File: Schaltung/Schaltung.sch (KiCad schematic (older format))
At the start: 18 parts

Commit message: new annotation
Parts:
- J1: renamed from J?; value Conn_01x02 -> Elektroden
- R1, R2: renamed from R?; value R -> 0,86
- gave numbers to parts that had none: 15
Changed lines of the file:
@@
 $EndDescr
 $Comp
-L +12V #PWR?
+L +12V #PWR1
 U 1 1 5ABA1DC9
 P 1650 1600
-F 0 "#PWR?" H 1650 1450 50  0001 C CNN
+F 0 "#PWR1" H 1650 1450 50  0001 C CNN
 F 1 "+12V" H 1650 1740 50  0000 C CNN
 F 2 "" H 1650 1600 50  0001 C CNN
@@
 $EndComp
 $Comp
-L GND #PWR?
+L GND #PWR4
 U 1 1 5ABA1DDD
 P 4000 2900
-F 0 "#PWR?" H 4000 2650 50  0001 C CNN
+F 0 "#PWR4" H 4000 2650 50  0001 C CNN
 F 1 "GND" H 4000 2750 50  0000 C CNN
 F 2 "" H 4000 2900 50  0001 C CNN
@@
 $EndComp
 $Comp
-L CP C?
+L CP C4
 U 1 1 5ABA1E01
 P 4000 2750
-F 0 "C?" H 4025 2850 50  0000 L CNN
+F 0 "C4" H 4025 2850 50  0000 L CNN
 F 1 "2F" H 4025 2650 50  0000 L CNN
 F 2 "" H 4038 2600 50  0001 C CNN
@@
 $EndComp
 $Comp
-L R R?
+L R R1
 U 1 1 5ABA1EAA
 P 2000 1600
-F 0 "R?" V 2080 1600 50  0000 C CNN
-F 1 "R" V 2000 1600 50  0000 C CNN
+F 0 "R1" V 2080 1600 50  0000 C CNN
+F 1 "0,86" V 2000 1600 50  0000 C CNN
 F 2 "" V 1930 1600 50  0001 C CNN
 F 3 "" H 2000 1600 50  0001 C CNN
@@
 $EndComp
 $Comp
-L R R?
+L R R2
 U 1 1 5ABA1F5B
 P 2400 1600
-F 0 "R?" V 2480 1600 50  0000 C CNN
-F 1 "R" V 2400 1600 50  0000 C CNN
+F 0 "R2" V 2480 1600 50  0000 C CNN
+F 1 "0,86" V 2400 1600 50  0000 C CNN
 F 2 "" V 2330 1600 50  0001 C CNN
 F 3 "" H 2400 1600 50  0001 C CNN
@@
 $EndComp
 $Comp
-L BUZ11 Q?
+L BUZ11 Q3
 U 1 1 5ABA2384
 P 5850 1800
-F 0 "Q?" H 6100 1875 50  0000 L CNN
+F 0 "Q3" H 6100 1875 50  0000 L CNN
 F 1 "IRF1404" H 6100 1800 50  0000 L CNN
 F 2 "TO_SOT_Packages_THT:TO-220_Vertical" H 6100 1725 50  0001 L CIN
@@
 $EndComp
 $Comp
-L BUZ11 Q?
+L BUZ11 Q4
 U 1 1 5ABA25E3
 P 5850 2300
-F 0 "Q?" H 6100 2375 50  0000 L CNN
+F 0 "Q4" H 6100 2375 50  0000 L CNN
 F 1 "IRF1404" H 6100 2300 50  0000 L CNN
 F 2 "TO_SOT_Packages_THT:TO-220_Vertical" H 6100 2225 50  0001 L CIN
@@
 $EndComp
 $Comp
-L BUZ11 Q?
+L BUZ11 Q5
 U 1 1 5ABA2633
 P 5850 2800
-F 0 "Q?" H 6100 2875 50  0000 L CNN
+F 0 "Q5" H 6100 2875 50  0000 L CNN
 F 1 "IRF1404" H 6100 2800 50  0000 L CNN
 F 2 "TO_SOT_Packages_THT:TO-220_Vertical" H 6100 2725 50  0001 L CIN
@@
 $EndComp
 $Comp
-L BUZ11 Q?
+L BUZ11 Q6
 U 1 1 5ABA2676
 P 5850 3300
-F 0 "Q?" H 6100 3375 50  0000 L CNN
+F 0 "Q6" H 6100 3375 50  0000 L CNN
 F 1 "IRF1404" H 6100 3300 50  0000 L CNN
 F 2 "TO_SOT_Packages_THT:TO-220_Vertical" H 6100 3225 50  0001 L CIN
@@
 $EndComp
 $Comp
-L BUZ11 Q?
+L BUZ11 Q7
 U 1 1 5ABA26B6
 P 5850 3800
-F 0 "Q?" H 6100 3875 50  0000 L CNN
+F 0 "Q7" H 6100 3875 50  0000 L CNN
 F 1 "IRF1404" H 6100 3800 50  0000 L CNN
 F 2 "TO_SOT_Packages_THT:TO-220_Vertical" H 6100 3725 50  0001 L CIN
@@
 $EndComp
 $Comp
-L BSS83P Q?
+L BSS83P Q1
 U 1 1 5ABA26EC
 P 3100 1800
-F 0 "Q?" H 3300 1875 50  0000 L CNN
+F 0 "Q1" H 3300 1875 50  0000 L CNN
 F 1 "IRF4905" H 3300 1800 50  0000 L CNN
 F 2 "TO_SOT_Packages_SMD:SOT-23" H 3300 1725 50  0001 L CIN
@@
 $EndComp
 $Comp
-L BSS83P Q?
+L BSS83P Q2
 U 1 1 5ABA2A57
 P 3100 2400
-F 0 "Q?" H 3300 2475 50  0000 L CNN
+F 0 "Q2" H 3300 2475 50  0000 L CNN
 F 1 "IRF4905" H 3300 2400 50  0000 L CNN
 F 2 "TO_SOT_Packages_SMD:SOT-23" H 3300 2325 50  0001 L CIN
@@
 	6600 2000 6600 4200
 $Comp
-L GND #PWR?
+L GND #PWR6
 U 1 1 5ABA3862
 P 6600 4200
-F 0 "#PWR?" H 6600 3950 50  0001 C CNN
+F 0 "#PWR6" H 6600 3950 50  0001 C CNN
 F 1 "GND" H 6600 4050 50  0000 C CNN
 F 2 "" H 6600 4200 50  0001 C CNN
@@
 Connection ~ 6600 2500
 $Comp
-L SW_Push SW?
+L SW_Push SW1
 U 1 1 5ABA3A3F
 P 4600 6400
-F 0 "SW?" H 4650 6500 50  0000 L CNN
+F 0 "SW1" H 4650 6500 50  0000 L CNN
 F 1 "SW_Push" H 4600 6340 50  0000 C CNN
 F 2 "" H 4600 6600 50  0001 C CNN
@@
 $EndComp
 $Comp
-L CP C?
+L CP C2
 U 1 1 5ABA3C2E
 P 3150 4850
-F 0 "C?" H 3175 4950 50  0000 L CNN
+F 0 "C2" H 3175 4950 50  0000 L CNN
 F 1 "100µF" H 3175 4750 50  0000 L CNN
 F 2 "" H 3188 4700 50  0001 C CNN
@@
 $EndComp
 $Comp
-L C C?
+L C C3
 U 1 1 5ABA3CD4
 P 3550 4850
-F 0 "C?" H 3575 4950 50  0000 L CNN
+F 0 "C3" H 3575 4950 50  0000 L CNN
 F 1 "100nF" H 3575 4750 50  0000 L CNN
 F 2 "" H 3588 4700 50  0001 C CNN
@@
 Connection ~ 5650 2300
 $Comp
-L GND #PWR?
+L GND #PWR3
 U 1 1 5ABA420C
 P 3350 5200
-F 0 "#PWR?" H 3350 4950 50  0001 C CNN
+F 0 "#PWR3" H 3350 4950 50  0001 C CNN
 F 1 "GND" H 3350 5050 50  0000 C CNN
 F 2 "" H 3350 5200 50  0001 C CNN
@@
 $EndComp
 $Comp
-L Conn_01x02 J?
+L Conn_01x02 J1
 U 1 1 5ABA428E
 P 4500 3050
-F 0 "J?" H 4500 3150 50  0000 C CNN
-F 1 "Conn_01x02" V 4650 3000 50  0000 C CNN
+F 0 "J1" H 4500 3150 50  0000 C CNN
+F 1 "Elektroden" V 4650 3000 50  0000 C CNN
 F 2 "" H 4500 3050 50  0001 C CNN
 F 3 "" H 4500 3050 50  0001 C CNN
@@
 	4600 4700 4600 4800
 $Comp
-L MIC4427 U?
+L MIC4427 U1
 U 1 1 5ABA4E0E
 P 4600 5300
-F 0 "U?" H 4500 5800 50  0000 R CNN
+F 0 "U1" H 4500 5800 50  0000 R CNN
 F 1 "TC4420" H 4500 5700 50  0000 R CNN
 F 2 "" H 4600 5000 50  0001 C CNN
@@
 	5650 5400 5200 5400
 $Comp
-L GND #PWR?
+L GND #PWR5
 U 1 1 5ABA514E
 P 4600 5800
-F 0 "#PWR?" H 4600 5550 50  0001 C CNN
+F 0 "#PWR5" H 4600 5550 50  0001 C CNN
 F 1 "GND" H 4600 5650 50  0000 C CNN
 F 2 "" H 4600 5800 50  0001 C CNN
@@
 Connection ~ 4000 5400
 $Comp
-L CP C?
+L CP C1
 U 1 1 5ABA57FA
 P 2400 5450
-F 0 "C?" H 2425 5550 50  0000 L CNN
+F 0 "C1" H 2425 5550 50  0000 L CNN
 F 1 "4,7µF" H 2425 5350 50  0000 L CNN
 F 2 "" H 2438 5300 50  0001 C CNN
@@
 $EndComp
 $Comp
-L GND #PWR?
+L GND #PWR2
 U 1 1 5ABA5807
 P 2400 5700
-F 0 "#PWR?" H 2400 5450 50  0001 C CNN
+F 0 "#PWR2" H 2400 5450 50  0001 C CNN
 F 1 "GND" H 2400 5550 50  0000 C CNN
 F 2 "" H 2400 5700 50  0001 C CNN
@@
 	4900 6400 4800 6400
 $Comp
-L D D?
+L D D2
 U 1 1 5ABA5BA8
 P 2800 4700
-F 0 "D?" H 2800 4800 50  0000 C CNN
+F 0 "D2" H 2800 4800 50  0000 C CNN
 F 1 "D" H 2800 4600 50  0000 C CNN
 F 2 "" H 2800 4700 50  0001 C CNN
@@
 $EndComp
 $Comp
-L D D?
+L D D1
 U 1 1 5ABA5C86
 P 2400 5050
-F 0 "D?" H 2400 5150 50  0000 C CNN
+F 0 "D1" H 2400 5150 50  0000 C CNN
 F 1 "D" H 2400 4950 50  0000 C CNN
 F 2 "" H 2400 5050 50  0001 C CNN

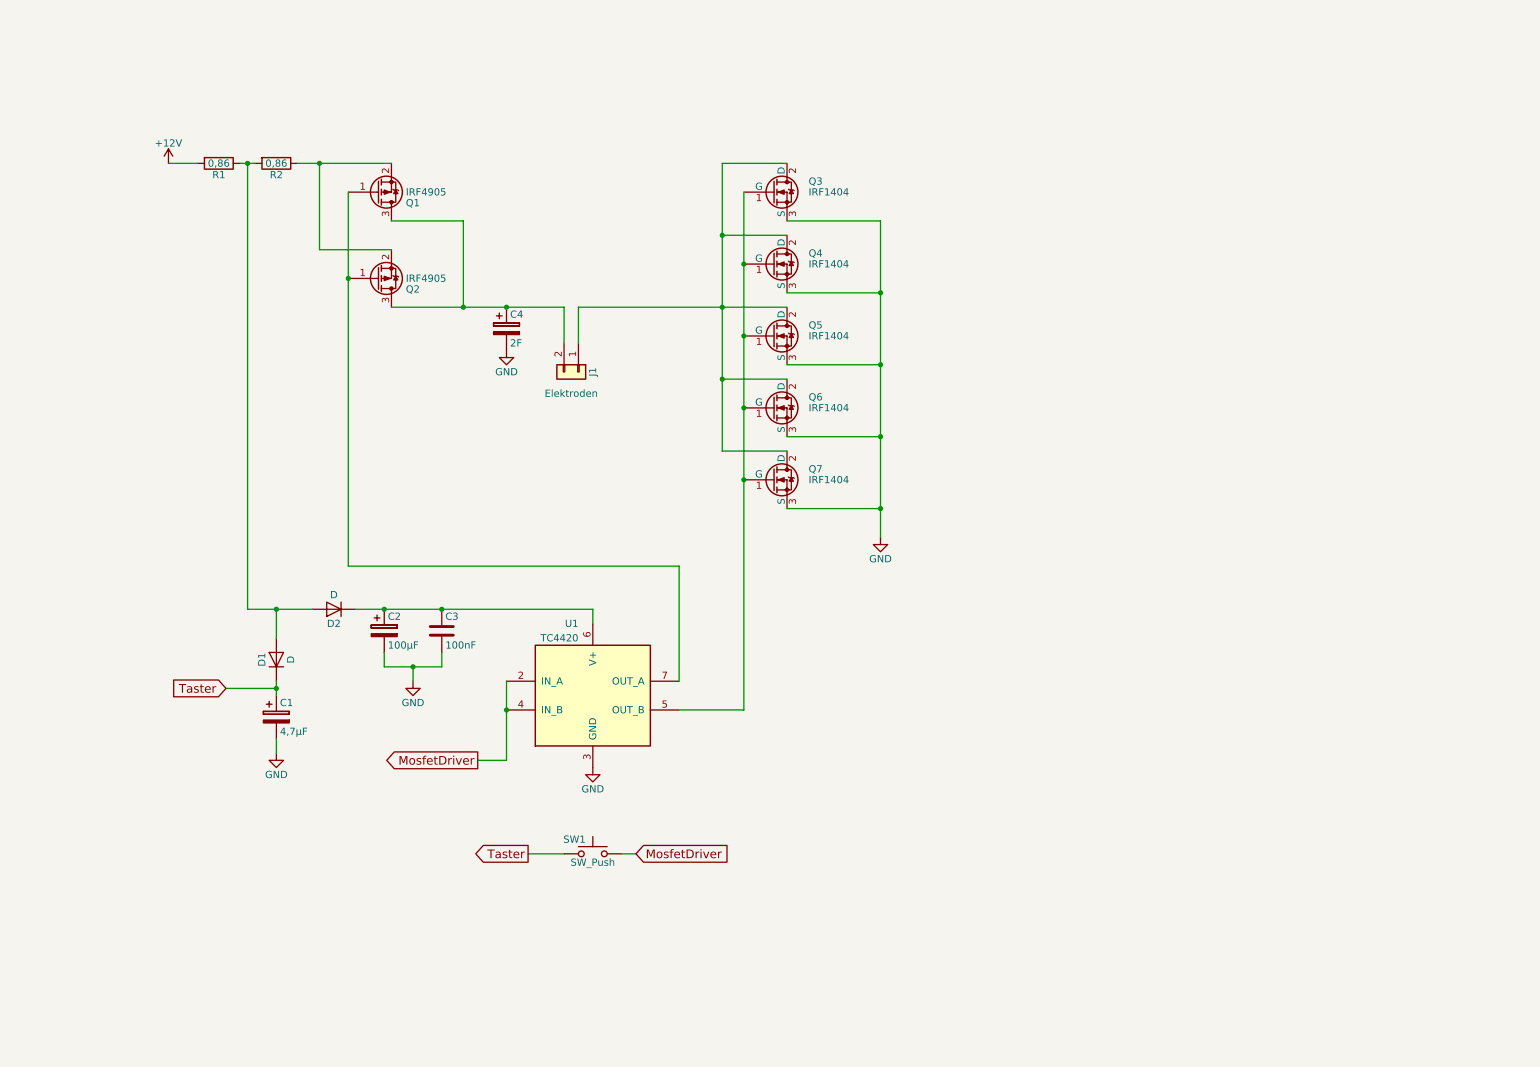
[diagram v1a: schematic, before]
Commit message: change to a concept with MC
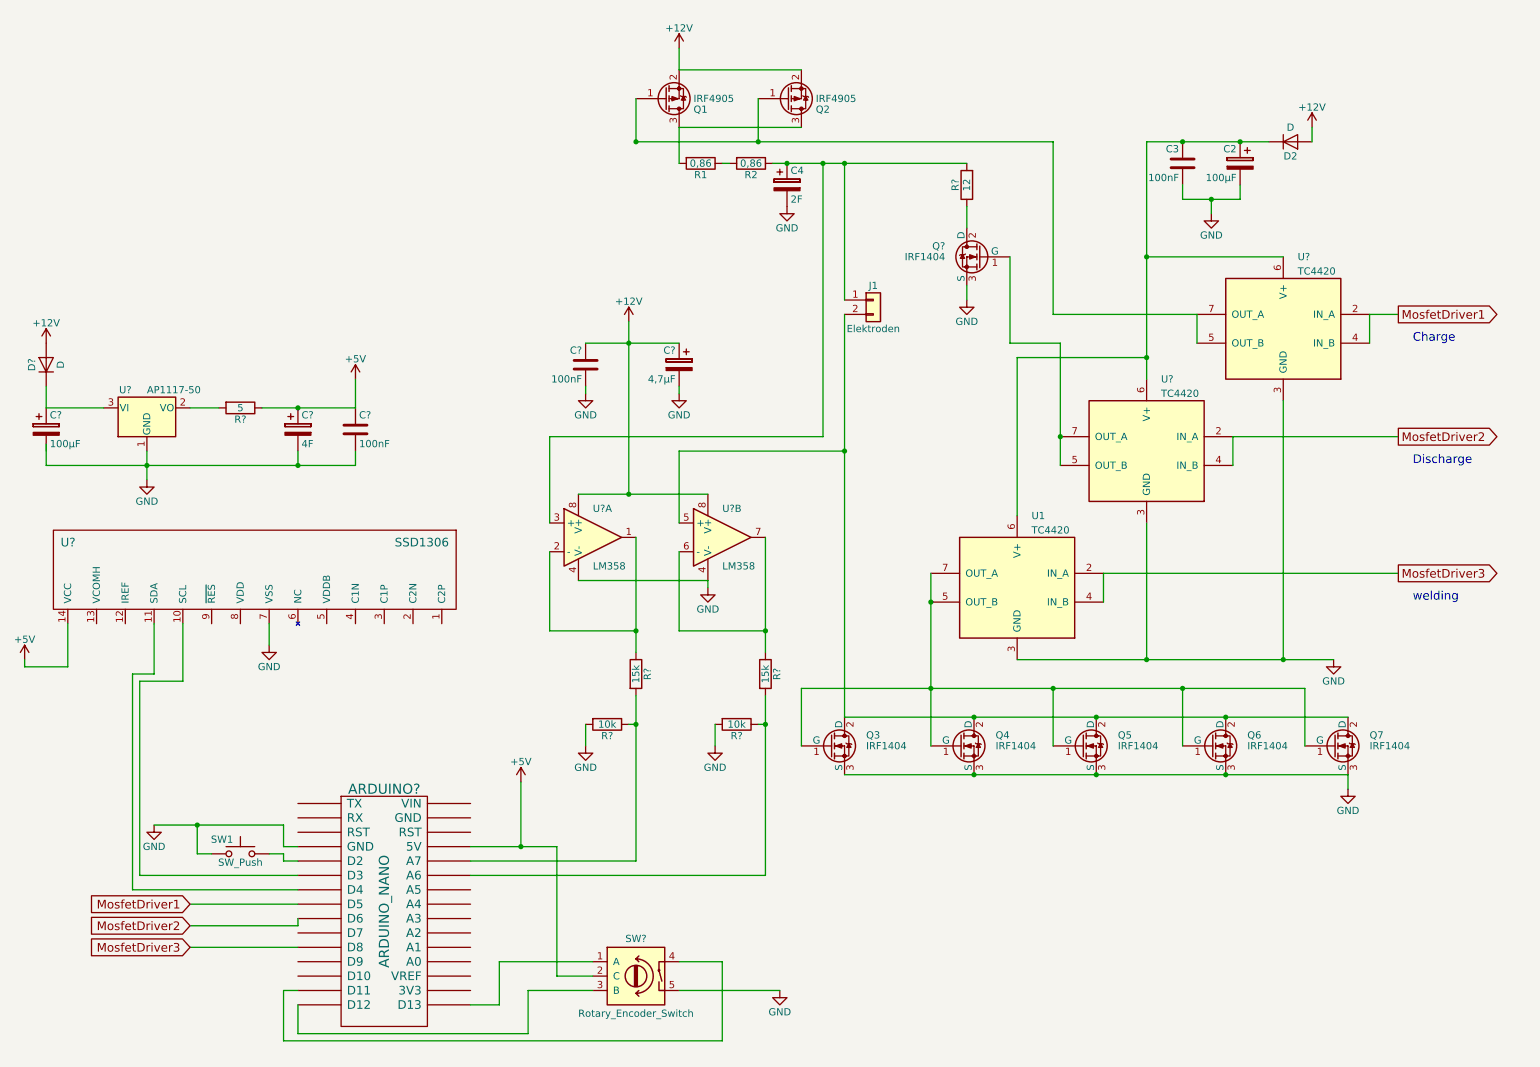
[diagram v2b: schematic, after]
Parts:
- removed C1: 4,7µF, symbol CP
- removed D1: D, symbol D
- added ARDUINO?: ARDUINO_NANO, symbol ARDUINO_NANO
- added C?: 100µF, symbol CP
- added C?: 4F, symbol CP
- added C? (x2): 100nF, symbol C
- added C?: 4,7µF, symbol CP
- added D?: D, symbol D
- added Q?: IRF1404, TO_SOT_Packages_THT:TO-220_Vertical, symbol BUZ11
- added R?: 5, symbol R
- added R?: 12, symbol R
- added R? (x2): 15k, symbol R
- added R? (x2): 10k, symbol R
- added SW?: Rotary_Encoder_Switch, symbol Rotary_Encoder_Switch
- added U? (x2): LM358, symbol LM358
- added U?: AP1117-50, TO_SOT_Packages_SMD:SOT-223-3Lead_TabPin2, symbol AP1117-50
- added U? (x2): TC4420, symbol MIC4427
- added U?: SSD1306, symbol SSD1306
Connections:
- net Taster is gone; now on net GND: SW1.2
- net +12V: now also D2.2 (A), Q1.2 (S), Q2.2 (S), C?.1, C?.1, D?.2 (A), U?.8 (V+), U?.8 (V+); no longer R1.2
- net GND: now also ARDUINO?.4 (GND), C?.2, C?.2, C?.2, C?.2, Q?.3 (S), R?.2, R?.2, SW?.5, U?.1 (GND), U?.3 (GND), U?.3 (GND), U?.4 (V-), U?.4 (V-), U?.7 (VSS)
- net at Q1.3 (D), Q2.3 (D): now also R1.2; no longer C4.1, J1.2 (Pin_2)
- net at R1.1, R2.2: no longer D2.2 (A)
- net at Q3.1 (G), Q4.1 (G), Q5.1 (G)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: now also U1.7 (OUT_A)
- net at Q3.2 (D), Q4.2 (D), Q5.2 (D)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: now also J1.2 (Pin_2), U?.5 (+); no longer J1.1 (Pin_1)
- net at Q1.1 (G), Q2.1 (G): now also U?.5 (OUT_B), U?.7 (OUT_A); no longer U1.7 (OUT_A)
- net at C2.1, C3.1, D2.1 (K)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: now also U?.6 (V+), U?.6 (V+)
- net MosfetDriver renamed MosfetDriver3
- net MosfetDriver3: now also ARDUINO?.11 (D8); no longer SW1.1
- new net: C4.1, J1.1 (Pin_1), R2.1, R?.2, U?.3 (+)
- new net: ARDUINO?.5 (D2), SW1.1
- new net: R?.1, U?.1, U?.2 (-)
- new net: R?.1, U?.6 (-), U?.7
- new net: ARDUINO?.14 (D11), SW?.4
- new net: ARDUINO?.15 (D12), SW?.3 (B)
- new net: ARDUINO?.16 (D13), SW?.1 (A)
- new net: ARDUINO?.25 (A6), R?.1, R?.2
- new net: ARDUINO?.26 (A7), R?.1, R?.2
- new net: ARDUINO?.6 (D3), U?.10 (SCL)
- new net: ARDUINO?.7 (D4), U?.11 (SDA)
- new net: R?.2, U?.2 (VO)
- new net: C?.1, D?.1 (K), U?.3 (VI)
- new net: Q?.2 (D), R?.1
- new net: Q?.1 (G), U?.5 (OUT_B), U?.7 (OUT_A)
- new net +5V: ARDUINO?.27 (5V), C?.1, C?.1, R?.1, SW?.2 (C), U?.14 (VCC)
- new net MosfetDriver1: ARDUINO?.8 (D5), U?.2 (IN_A), U?.4 (IN_B)
- new net MosfetDriver2: ARDUINO?.9 (D6), U?.2 (IN_A), U?.4 (IN_B)
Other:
- note added: "Charge"
- note added: "Discharge"
- note added: "welding"
- moved on the sheet: C2, C3, C4, D2, J1, Q1, Q2, Q3, Q4, Q5, Q6, Q7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
